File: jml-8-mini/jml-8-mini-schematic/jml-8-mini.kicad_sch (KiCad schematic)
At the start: 3 parts, among them J1 Barrel_Jack, SW1 SW_DPDT_x2, U1 Z80CPU

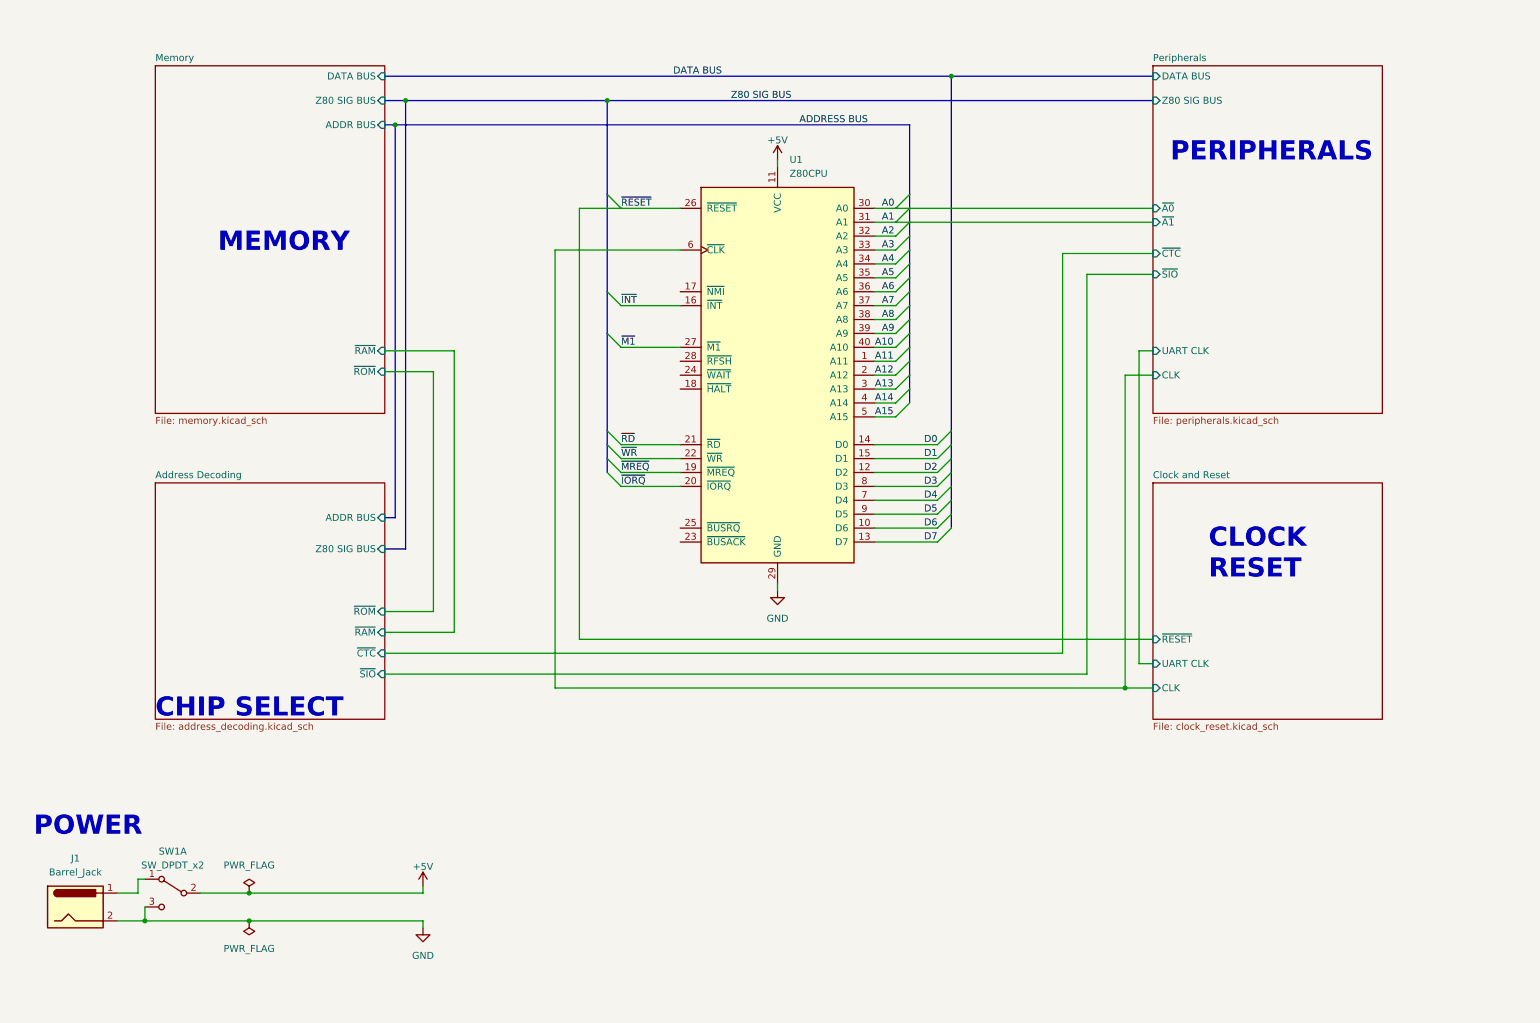
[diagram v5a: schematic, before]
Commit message: lots of changes to schematic, redone to make easier to read and add to
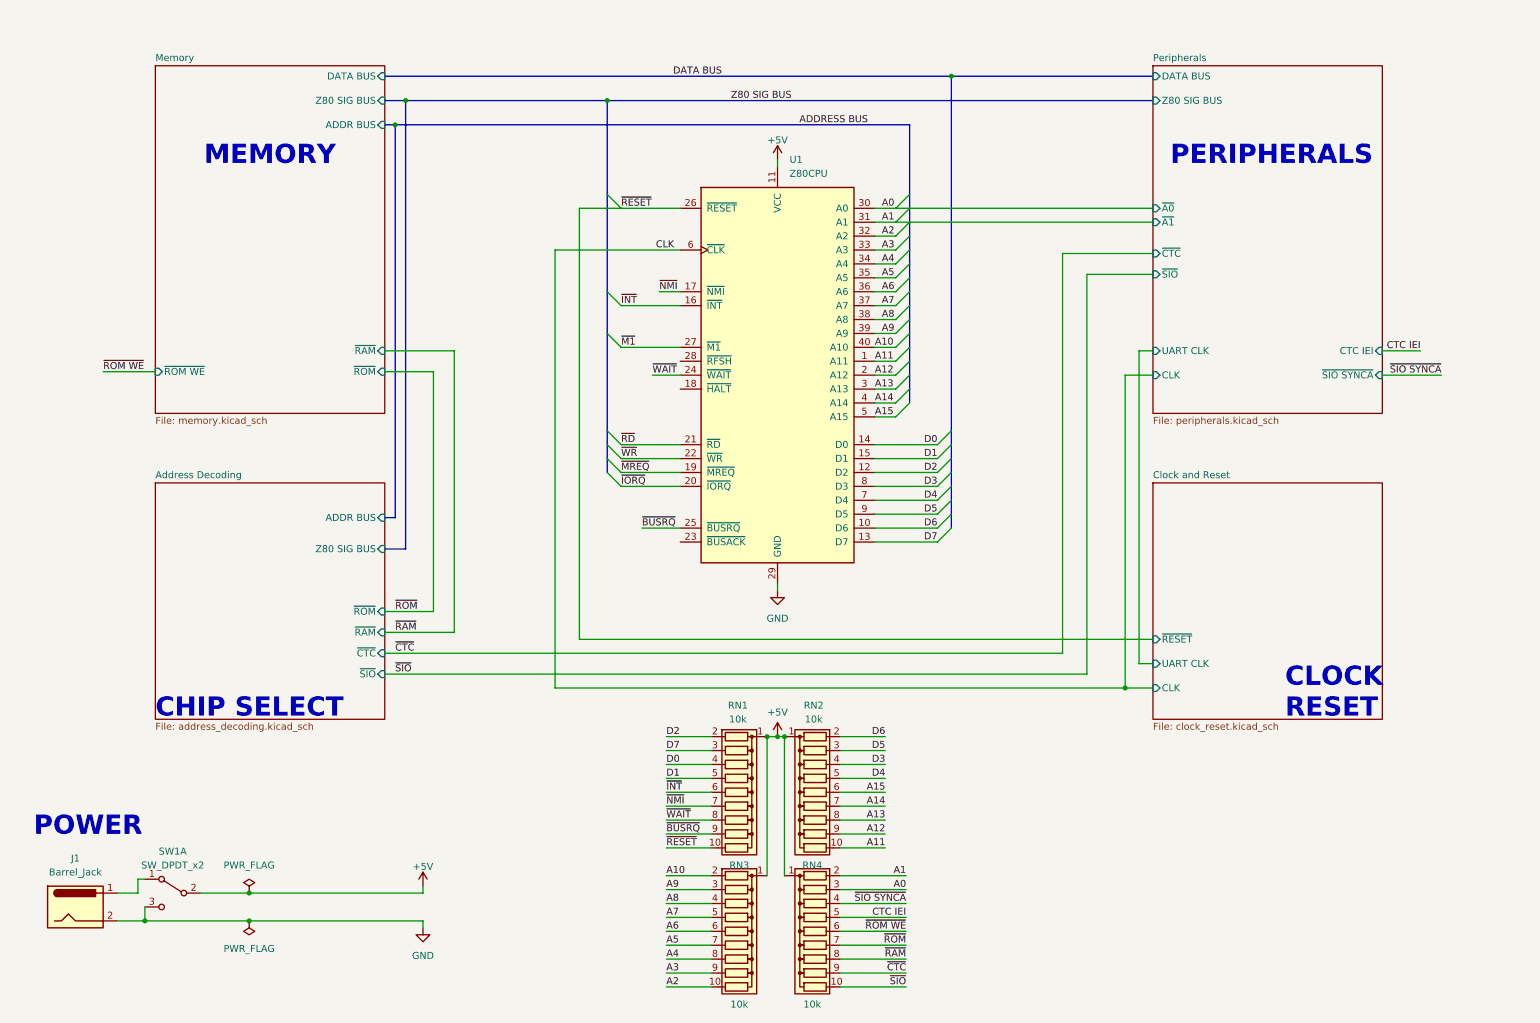
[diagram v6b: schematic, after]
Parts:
- added RN1, RN2, RN3, RN4: 10k, Resistor_THT:R_Array_SIP10, symbol Device:R_Network09
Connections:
- net +5V: now also RN1.1 (common), RN2.1 (common), RN3.1 (common), RN4.1 (common)
- net A0: now also RN4.3 (R2)
- net A1: now also RN4.2 (R1)
- net A10: now also RN3.2 (R1)
- net A11: now also RN2.10 (R9)
- net A12: now also RN2.9 (R8)
- net A13: now also RN2.8 (R7)
- net A14: now also RN2.7 (R6)
- net A15: now also RN2.6 (R5)
- net A2: now also RN3.10 (R9)
- net A3: now also RN3.9 (R8)
- net A4: now also RN3.8 (R7)
- net A5: now also RN3.7 (R6)
- net A6: now also RN3.6 (R5)
- net A7: now also RN3.5 (R4)
- net A8: now also RN3.4 (R3)
- net A9: now also RN3.3 (R2)
- net D0: now also RN1.4 (R3)
- net D1: now also RN1.5 (R4)
- net D2: now also RN1.2 (R1)
- net D3: now also RN2.4 (R3)
- net D4: now also RN2.5 (R4)
- net D5: now also RN2.3 (R2)
- net D6: now also RN2.2 (R1)
- net D7: now also RN1.3 (R2)
- net ~{INT}: now also RN1.6 (R5)
- net ~{RESET}: now also RN1.10 (R9)
- net ~{NMI}: now reaches U1.17 (~{NMI})
- net ~{NMI}: now also RN1.7 (R6)
- net ~{WAIT}: now reaches U1.24 (~{WAIT})
- net ~{WAIT}: now also RN1.8 (R7)
- net ~{BUSRQ}: now reaches U1.25 (~{BUSRQ})
- net ~{BUSRQ}: now also RN1.9 (R8)
- net Clock and Reset/CLK renamed CLK
- new net CTC IEI: RN4.5 (R4)
- new net ~{CTC}: RN4.9 (R8)
- new net ~{RAM}: RN4.8 (R7)
- new net ~{ROM WE}: RN4.6 (R5)
- new net ~{ROM}: RN4.7 (R6)
- new net ~{SIO SYNCA}: RN4.4 (R3)
- new net ~{SIO}: RN4.10 (R9)
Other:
- sheet Memory ports: added ~{ROM WE}; removed none
- sheet Peripherals ports: added CTC IEI, ~{SIO SYNCA}; removed none

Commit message: minor updates to schematic
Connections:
- no-connect marks 0 -> 3
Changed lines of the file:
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@@
   (junction (at 151.13 147.955) (diameter 0) (color 0 0 0 0)
   )
+  (no_connect (at 132.08 84.455))
+  (no_connect (at 132.08 79.375))
+  (no_connect (at 132.08 112.395))
   (bus_entry (at 118.745 97.155) (size 2.54 2.54)
     (stroke (width 0) (type default))

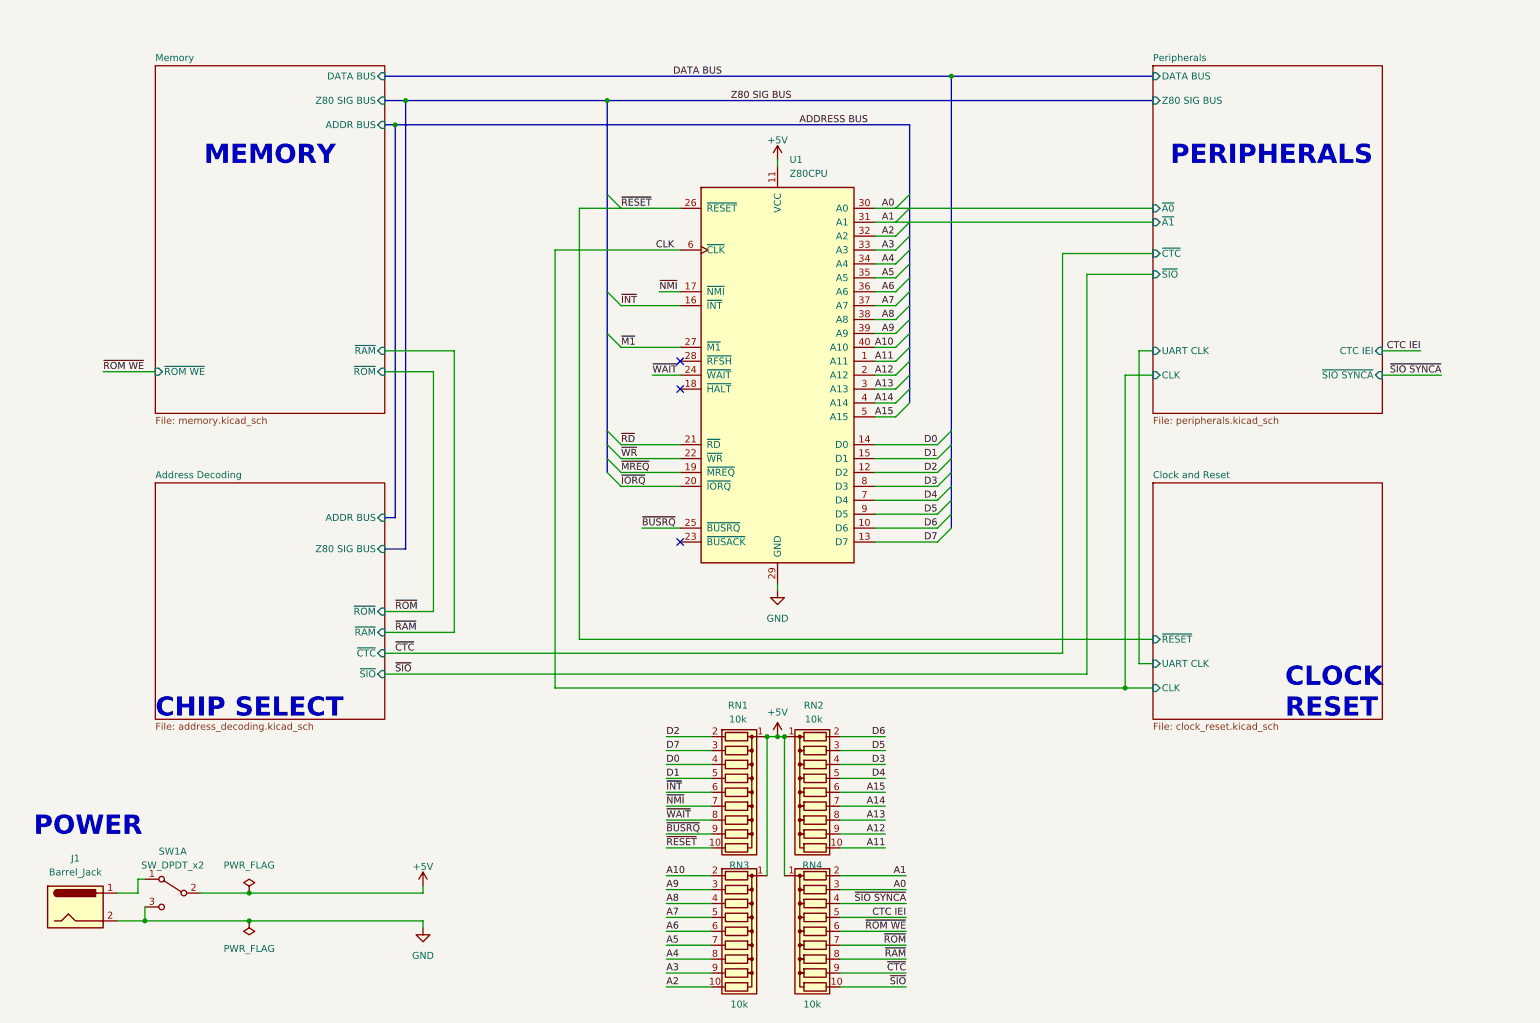
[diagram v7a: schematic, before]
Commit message: complete schematic
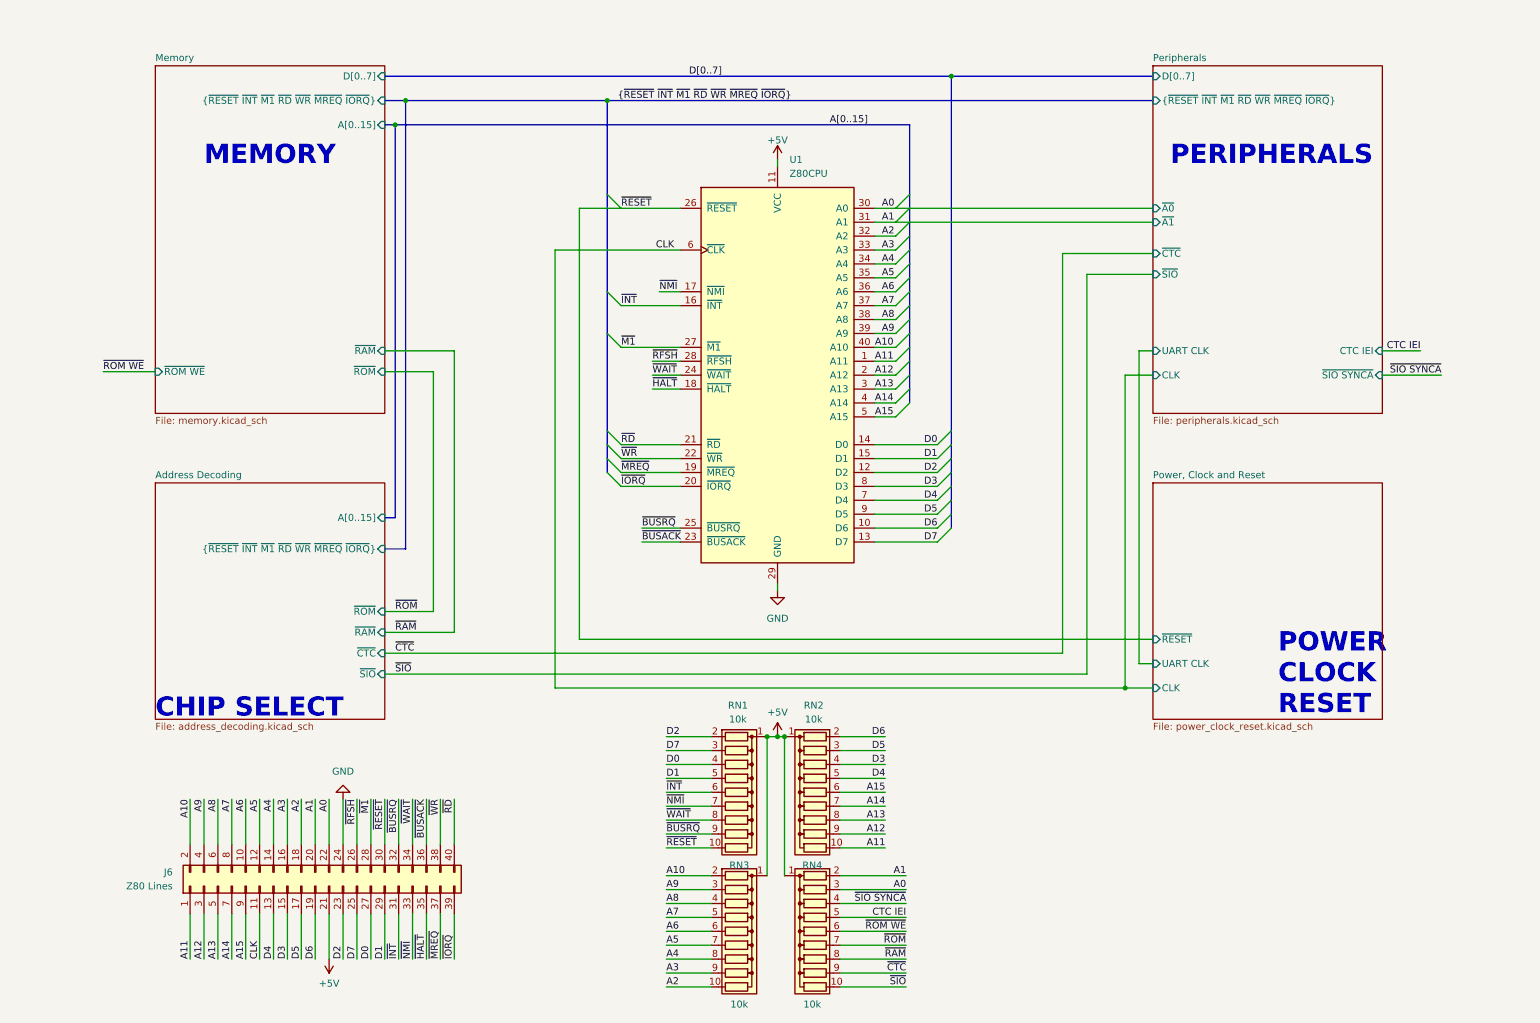
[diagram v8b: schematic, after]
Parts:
- removed J1: Barrel_Jack, Connector_BarrelJack:BarrelJack_Horizontal, symbol Connector:Barrel_Jack
- removed SW1: SW_DPDT_x2, symbol Switch:SW_DPDT_x2
- added J6: Z80 Lines, Connector_PinHeader_2.54mm:PinHeader_2x20_P2.54mm_Vertical, symbol Connector_Generic:Conn_02x20_Odd_Even
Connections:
- net +5V: now also J6.21 (Pin_21)
- net A0: now also J6.22 (Pin_22)
- net A1: now also J6.20 (Pin_20)
- net A10: now also J6.2 (Pin_2)
- net A11: now also J6.1 (Pin_1)
- net A12: now also J6.3 (Pin_3)
- net A13: now also J6.5 (Pin_5)
- net A14: now also J6.7 (Pin_7)
- net A15: now also J6.9 (Pin_9)
- net A2: now also J6.18 (Pin_18)
- net A3: now also J6.16 (Pin_16)
- net A4: now also J6.14 (Pin_14)
- net A5: now also J6.12 (Pin_12)
- net A6: now also J6.10 (Pin_10)
- net A7: now also J6.8 (Pin_8)
- net A8: now also J6.6 (Pin_6)
- net A9: now also J6.4 (Pin_4)
- net CLK: now also J6.11 (Pin_11)
- net D0: now also J6.27 (Pin_27)
- net D1: now also J6.29 (Pin_29)
- net D2: now also J6.23 (Pin_23)
- net D3: now also J6.15 (Pin_15)
- net D4: now also J6.13 (Pin_13)
- net D5: now also J6.17 (Pin_17)
- net D6: now also J6.19 (Pin_19)
- net D7: now also J6.25 (Pin_25)
- net GND: now also J6.24 (Pin_24)
- net ~{BUSRQ}: now also J6.32 (Pin_32)
- net ~{INT}: now also J6.31 (Pin_31)
- net ~{IORQ}: now also J6.39 (Pin_39)
- net ~{M1}: now also J6.28 (Pin_28)
- net ~{MREQ}: now also J6.37 (Pin_37)
- net ~{NMI}: now also J6.33 (Pin_33)
- net ~{RD}: now also J6.40 (Pin_40)
- net ~{RESET}: now also J6.30 (Pin_30)
- net ~{WAIT}: now also J6.34 (Pin_34)
- net ~{WR}: now also J6.38 (Pin_38)
- net ~{HALT}: now reaches U1.18 (~{HALT})
- net ~{HALT}: now also J6.35 (Pin_35)
- net ~{BUSACK}: now reaches U1.23 (~{BUSACK})
- net ~{BUSACK}: now also J6.36 (Pin_36)
- net ~{RFSH}: now reaches U1.28 (~{RFSH})
- net ~{RFSH}: now also J6.26 (Pin_26)
- no-connect marks 3 -> 0
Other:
- sheet Clock and Reset renamed Power, Clock and Reset
- sheet Address Decoding ports: added A[0..15], {~{RESET} ~{INT} ~{M1} ~{RD} ~{WR} ~{MREQ} ~{IORQ}}; removed ADDR BUS, Z80 SIG BUS
- sheet Memory ports: added A[0..15], D[0..7], {~{RESET} ~{INT} ~{M1} ~{RD} ~{WR} ~{MREQ} ~{IORQ}}; removed ADDR BUS, DATA BUS, Z80 SIG BUS
- sheet Peripherals ports: added D[0..7], {~{RESET} ~{INT} ~{M1} ~{RD} ~{WR} ~{MREQ} ~{IORQ}}; removed DATA BUS, Z80 SIG BUS
- sheet Power, Clock and Reset: file clock_reset.kicad_sch -> power_clock_reset.kicad_sch
- note added: "POWER CLOCK RESET"
- note removed: "CLOCK RESET"
- note removed: "POWER"
